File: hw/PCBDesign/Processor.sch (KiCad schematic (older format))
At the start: 39 parts, among them J4 Conn_ARM_JTAG_SWD_10, U11 74HC595, U13 STM32F446RETx, Y1 8MHz Crystal

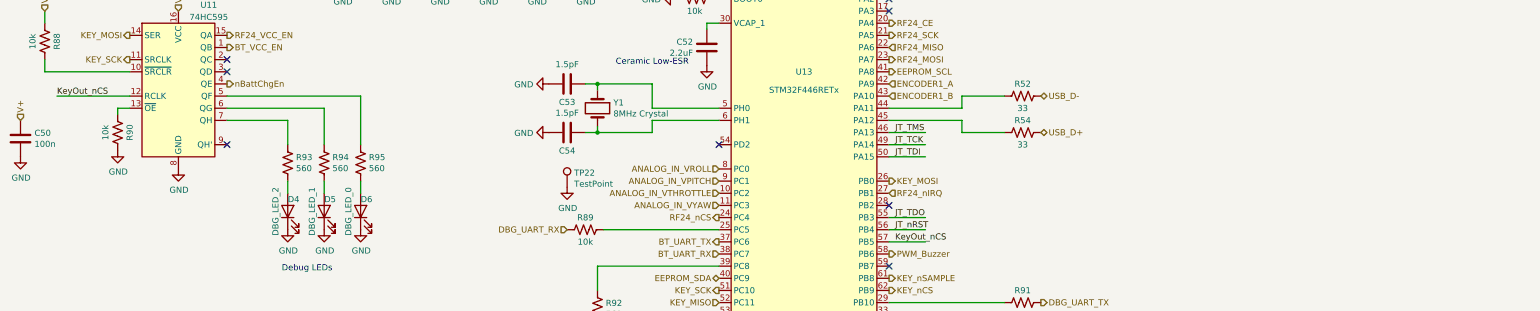
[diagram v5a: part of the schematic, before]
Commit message: Investigate some USB issues. Add PCB remarks for revision 2
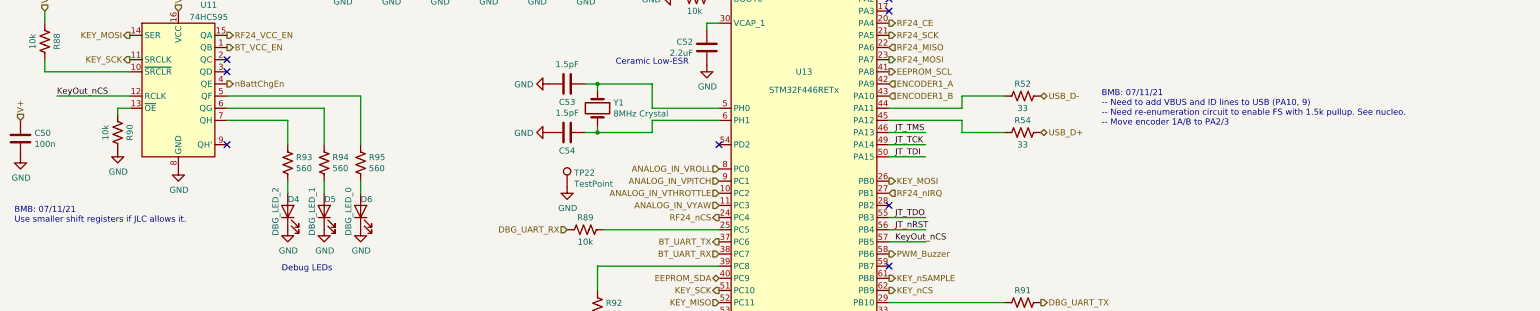
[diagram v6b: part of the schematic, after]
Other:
- note added: "BMB: 07/11/21\n-- Need to add VBUS and ID lines to USB (PA10, 9)\n-- Need re-enumeration circuit to enable FS with 1.5k pullup. See nucleo.\n-- Move encoder 1A/B to PA2/3"
- note added: "BMB: 07/11/21\nUse smaller shift registers if JLC allows it."
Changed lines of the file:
@@
 EELAYER 30 0
 EELAYER END
-$Descr A4 11693 8268
+$Descr A3 16535 11693
 encoding utf-8
 Sheet 11 11
@@
 Comment4 ""
 $EndDescr
-$Comp
-L MCU_ST_STM32F4:STM32F446RETx U13
-U 1 1 6047114C
-P 8100 2900
-F 0 "U13" H 8100 3600 50  0000 C CNN
-F 1 "STM32F446RETx" H 8100 3450 50  0000 C CNN
-F 2 "Package_QFP:LQFP-64_10x10mm_P0.5mm" H 7500 1200 50  0001 R CNN
-F 3 "http://www.st.com/st-web-ui/static/active/en/resource/technical/document/datasheet/DM00141306.pdf" H 8100 2900 50  0001 C CNN
-F 4 "C69336" H 8100 2900 50  0001 C CNN "LCSC"
-	1    8100 2900
-	1    0    0    -1
-$EndComp
 $Comp
 L Connector:Conn_ARM_JTAG_SWD_10 J4
@@
 Wire Wire Line
 	10200 6300 10200 6350
-$Comp
-L power:GND #PWR0106
-U 1 1 605ADCEE
-P 8100 4800
-F 0 "#PWR0106" H 8100 4550 50  0001 C CNN
-F 1 "GND" H 8105 4627 50  0000 C CNN
-F 2 "" H 8100 4800 50  0001 C CNN
-F 3 "" H 8100 4800 50  0001 C CNN
-	1    8100 4800
-	1    0    0    -1
-$EndComp
-Wire Wire Line
-	8100 4700 8100 4750
-Wire Wire Line
-	8100 4750 8200 4750
-Wire Wire Line
-	8200 4750 8200 4700
-Connection ~ 8100 4750
-Wire Wire Line
-	8100 4750 8100 4800
-Wire Wire Line
-	8200 4750 8300 4750
-Wire Wire Line
-	8300 4750 8300 4700
-Connection ~ 8200 4750
-Wire Wire Line
-	8100 4750 8000 4750
-Wire Wire Line
-	8000 4750 8000 4700
-Wire Wire Line
-	8000 4750 7900 4750
-Wire Wire Line
-	7900 4750 7900 4700
-Connection ~ 8000 4750
 Text Label 10750 5350 0    50   ~ 0
 JT_nRST
@@
 Text HLabel 8400 1100 1    50   Input ~ 0
 VDDA
-Wire Wire Line
-	8400 1100 8400 1200
 $Comp
 L Device:R_US R96
@@
 	9400 2500 8800 2500
 NoConn ~ 7400 4400
-NoConn ~ 7400 4500
 NoConn ~ 8800 3800
 NoConn ~ 8800 3300
@@
 NoConn ~ 3350 2200
 NoConn ~ 3350 2100
+Wire Wire Line
+	8400 1100 8400 1200
+NoConn ~ 7400 4500
+Connection ~ 8000 4750
+Wire Wire Line
+	7900 4750 7900 4700
+Wire Wire Line
+	8000 4750 7900 4750
+Wire Wire Line
+	8000 4750 8000 4700
+Wire Wire Line
+	8100 4750 8000 4750
+Connection ~ 8200 4750
+Wire Wire Line
+	8300 4750 8300 4700
+Wire Wire Line
+	8200 4750 8300 4750
+Wire Wire Line
+	8100 4750 8100 4800
+Connection ~ 8100 4750
+Wire Wire Line
+	8200 4750 8200 4700
+Wire Wire Line
+	8100 4750 8200 4750
+Wire Wire Line
+	8100 4700 8100 4750
+$Comp
+L power:GND #PWR0106
+U 1 1 605ADCEE
+P 8100 4800
+F 0 "#PWR0106" H 8100 4550 50  0001 C CNN
+F 1 "GND" H 8105 4627 50  0000 C CNN
+F 2 "" H 8100 4800 50  0001 C CNN
+F 3 "" H 8100 4800 50  0001 C CNN
+	1    8100 4800
+	1    0    0    -1
+$EndComp
+$Comp
+L MCU_ST_STM32F4:STM32F446RETx U13
+U 1 1 6047114C
+P 8100 2900
+F 0 "U13" H 8100 3600 50  0000 C CNN
+F 1 "STM32F446RETx" H 8100 3450 50  0000 C CNN
+F 2 "Package_QFP:LQFP-64_10x10mm_P0.5mm" H 7500 1200 50  0001 R CNN
+F 3 "http://www.st.com/st-web-ui/static/active/en/resource/technical/document/datasheet/DM00141306.pdf" H 8100 2900 50  0001 C CNN
+F 4 "C69336" H 8100 2900 50  0001 C CNN "LCSC"
+	1    8100 2900
+	1    0    0    -1
+$EndComp
+Text Notes 10550 2650 0    50   ~ 0
+BMB: 07/11/21\n-- Need to add VBUS and ID lines to USB (PA10, 9)\n-- Need re-enumeration circuit to enable FS with 1.5k pullup. See nucleo.\n-- Move encoder 1A/B to PA2/3
+Text Notes 1600 3450 0    50   ~ 0
+BMB: 07/11/21\nUse smaller shift registers if JLC allows it.
 $EndSCHEMATC

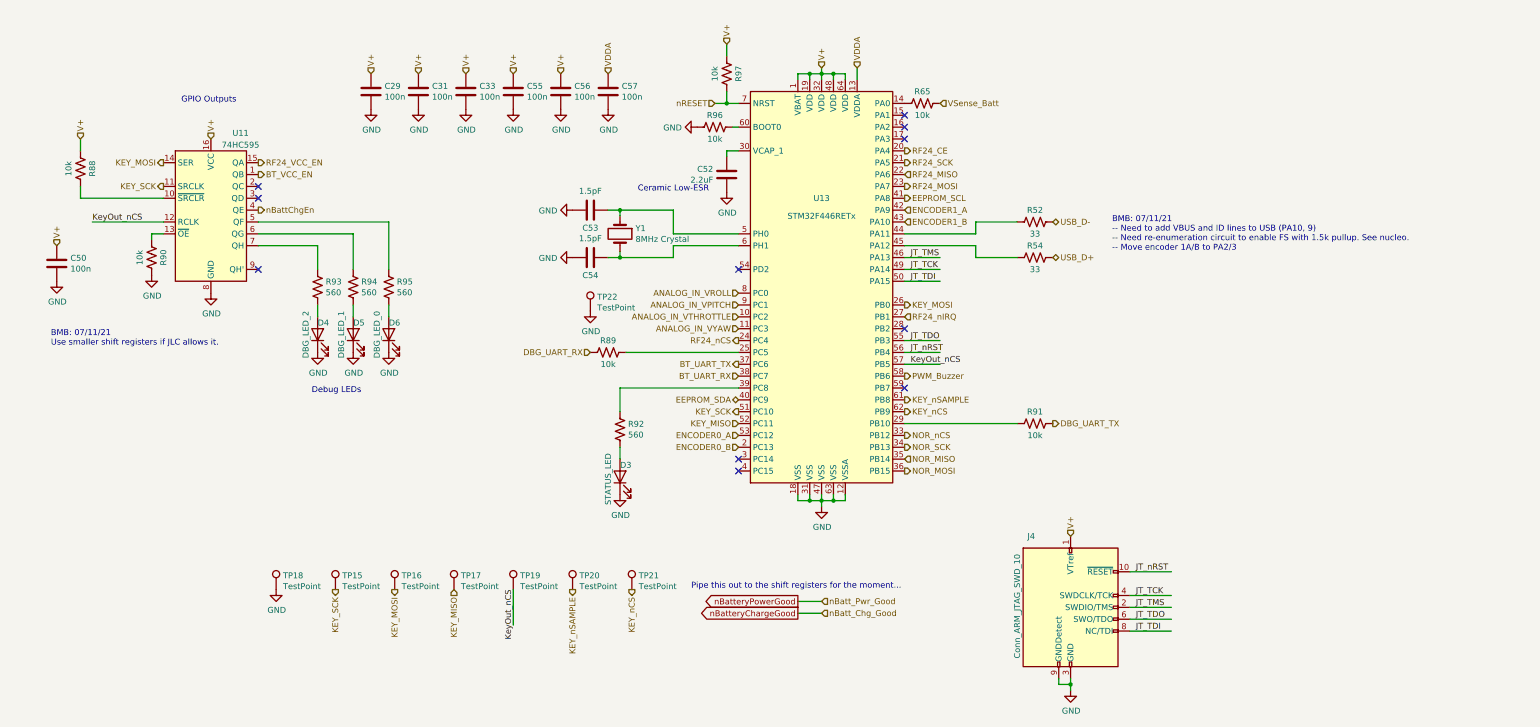
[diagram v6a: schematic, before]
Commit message: Start working on PCB rev 2.0
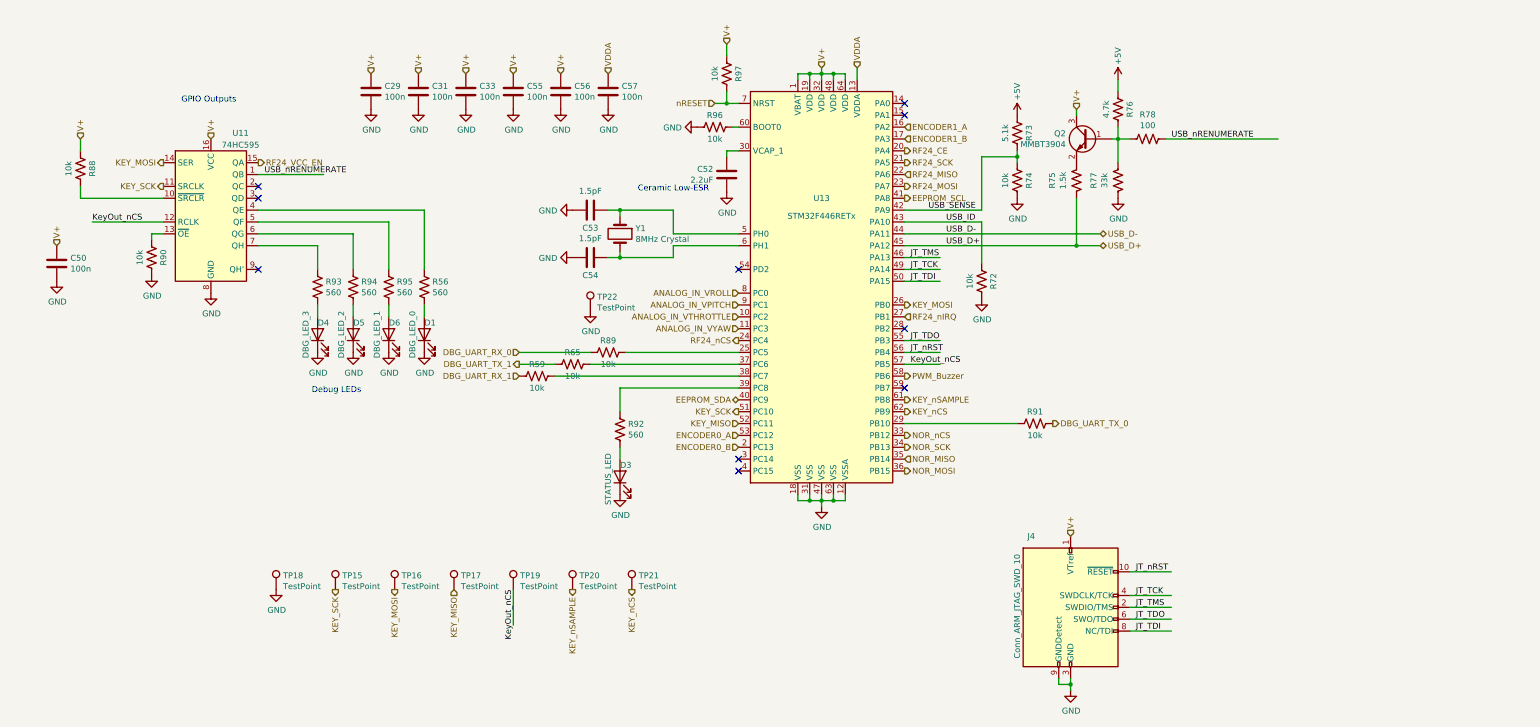
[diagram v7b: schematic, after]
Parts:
- removed R52, R54: 33, Resistor_SMD:R_0402_1005Metric, symbol Device:R_US
- added D1: DBG_LED_0, LED_SMD:LED_0603_1608Metric, symbol Device:LED
- added Q2: MMBT3904, Package_TO_SOT_SMD:SOT-23, symbol Transistor_BJT:MMBT3904
- added R56: 560, Resistor_SMD:R_0402_1005Metric, symbol Device:R_US
- added R59, R72, R74: 10k, Resistor_SMD:R_0402_1005Metric, symbol Device:R_US
- added R73: 5.1k, Resistor_SMD:R_0402_1005Metric, symbol Device:R_US
- added R75: 1.5k, Resistor_SMD:R_0402_1005Metric, symbol Device:R_US
- added R76: 4.7k, Resistor_SMD:R_0402_1005Metric, symbol Device:R_US
- added R77: 33k, Resistor_SMD:R_0402_1005Metric, symbol Device:R_US
- added R78: 100, Resistor_SMD:R_0402_1005Metric, symbol Device:R_US
- D4: value DBG_LED_2 -> DBG_LED_3
- D5: value DBG_LED_1 -> DBG_LED_2
- D6: value DBG_LED_0 -> DBG_LED_1
- J4: DigiKey (none) -> 609-3695-1-ND
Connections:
- net labels added: +5V, DBG_UART_RX_0, DBG_UART_RX_1, DBG_UART_TX_0, DBG_UART_TX_1, USB_ID, USB_SENSE, USB_nRENUMERATE
- net labels removed: BT_UART_RX, BT_UART_TX, BT_VCC_EN, DBG_UART_RX, DBG_UART_TX, VSense_Batt, nBattChgEn, nBatt_Chg_Good, nBatt_Pwr_Good, nBatteryChargeGood, nBatteryPowerGood
- wire segments 82 -> 100
- no-connect marks 11 -> 10
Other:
- note removed: "BMB: 07/11/21\n-- Need to add VBUS and ID lines to USB (PA10, 9)\n-- Need re-enumeration circuit to enable FS with 1.5k pullup. See nucleo.\n-- Move encoder 1A/B to PA2/3"
- note removed: "BMB: 07/11/21\nUse smaller shift registers if JLC allows it."
- note removed: "Pipe this out to the shift registers for the moment..."

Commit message: Add more work on PCB v2 design
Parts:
- removed TP15, TP16, TP17, TP18, TP19, TP20, TP21, TP22: TestPoint, TestPoint:TestPoint_Pad_2.5x2.5mm, symbol Connector:TestPoint
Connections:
- wire segments 100 -> 99
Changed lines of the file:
@@
 	6450 3500 7400 3500
-$Comp
-L Connector:TestPoint TP?
-U 1 1 605CFE2B
-P 3500 5500
-AR Path="/6045890B/605CFE2B" Ref="TP?"  Part="1"
-AR Path="/604707FB/605CFE2B" Ref="TP18"  Part="1"
-F 0 "TP18" H 3558 5618 50  0000 L CNN
-F 1 "TestPoint" H 3558 5527 50  0000 L CNN
-F 2 "TestPoint:TestPoint_Pad_2.5x2.5mm" H 3700 5500 50  0001 C CNN
-F 3 "~" H 3700 5500 50  0001 C CNN
-	1    3500 5500
-	1    0    0    -1
-$EndComp
-$Comp
-L power:GND #PWR09
-U 1 1 605D1BD5
-P 3500 5500
-F 0 "#PWR09" H 3500 5250 50  0001 C CNN
-F 1 "GND" H 3505 5327 50  0000 C CNN
-F 2 "" H 3500 5500 50  0001 C CNN
-F 3 "" H 3500 5500 50  0001 C CNN
-	1    3500 5500
-	1    0    0    -1
-$EndComp
-$Comp
-L Connector:TestPoint TP?
-U 1 1 605D1DEB
-P 4000 5500
-AR Path="/6045890B/605D1DEB" Ref="TP?"  Part="1"
-AR Path="/604707FB/605D1DEB" Ref="TP15"  Part="1"
-F 0 "TP15" H 4058 5618 50  0000 L CNN
-F 1 "TestPoint" H 4058 5527 50  0000 L CNN
-F 2 "TestPoint:TestPoint_Pad_2.5x2.5mm" H 4200 5500 50  0001 C CNN
-F 3 "~" H 4200 5500 50  0001 C CNN
-	1    4000 5500
-	1    0    0    -1
-$EndComp
-$Comp
-L Connector:TestPoint TP?
-U 1 1 605D20E0
-P 4500 5500
-AR Path="/6045890B/605D20E0" Ref="TP?"  Part="1"
-AR Path="/604707FB/605D20E0" Ref="TP16"  Part="1"
-F 0 "TP16" H 4558 5618 50  0000 L CNN
-F 1 "TestPoint" H 4558 5527 50  0000 L CNN
-F 2 "TestPoint:TestPoint_Pad_2.5x2.5mm" H 4700 5500 50  0001 C CNN
-F 3 "~" H 4700 5500 50  0001 C CNN
-	1    4500 5500
-	1    0    0    -1
-$EndComp
-$Comp
-L Connector:TestPoint TP?
-U 1 1 605D227A
-P 5000 5500
-AR Path="/6045890B/605D227A" Ref="TP?"  Part="1"
-AR Path="/604707FB/605D227A" Ref="TP17"  Part="1"
-F 0 "TP17" H 5058 5618 50  0000 L CNN
-F 1 "TestPoint" H 5058 5527 50  0000 L CNN
-F 2 "TestPoint:TestPoint_Pad_2.5x2.5mm" H 5200 5500 50  0001 C CNN
-F 3 "~" H 5200 5500 50  0001 C CNN
-	1    5000 5500
-	1    0    0    -1
-$EndComp
-$Comp
-L Connector:TestPoint TP?
-U 1 1 605D23A2
-P 5500 5500
-AR Path="/6045890B/605D23A2" Ref="TP?"  Part="1"
-AR Path="/604707FB/605D23A2" Ref="TP19"  Part="1"
-F 0 "TP19" H 5558 5618 50  0000 L CNN
-F 1 "TestPoint" H 5558 5527 50  0000 L CNN
-F 2 "TestPoint:TestPoint_Pad_2.5x2.5mm" H 5700 5500 50  0001 C CNN
-F 3 "~" H 5700 5500 50  0001 C CNN
-	1    5500 5500
-	1    0    0    -1
-$EndComp
-Text HLabel 4500 5500 3    50   Output ~ 0
-KEY_MOSI
-Text HLabel 5000 5500 3    50   Input ~ 0
-KEY_MISO
-Text HLabel 4000 5500 3    50   Output ~ 0
-KEY_SCK
-Text Label 5500 5500 3    50   ~ 0
-KeyOut_nCS
-Wire Wire Line
-	5500 5500 5500 5800
-$Comp
-L Connector:TestPoint TP?
-U 1 1 605D756E
-P 6000 5500
-AR Path="/6045890B/605D756E" Ref="TP?"  Part="1"
-AR Path="/604707FB/605D756E" Ref="TP20"  Part="1"
-F 0 "TP20" H 6058 5618 50  0000 L CNN
-F 1 "TestPoint" H 6058 5527 50  0000 L CNN
-F 2 "TestPoint:TestPoint_Pad_2.5x2.5mm" H 6200 5500 50  0001 C CNN
-F 3 "~" H 6200 5500 50  0001 C CNN
-	1    6000 5500
-	1    0    0    -1
-$EndComp
-Text HLabel 6000 5500 3    50   Output ~ 0
-KEY_nSAMPLE
-$Comp
-L Connector:TestPoint TP?
-U 1 1 605D9B3F
-P 6500 5500
-AR Path="/6045890B/605D9B3F" Ref="TP?"  Part="1"
-AR Path="/604707FB/605D9B3F" Ref="TP21"  Part="1"
-F 0 "TP21" H 6558 5618 50  0000 L CNN
-F 1 "TestPoint" H 6558 5527 50  0000 L CNN
-F 2 "TestPoint:TestPoint_Pad_2.5x2.5mm" H 6700 5500 50  0001 C CNN
-F 3 "~" H 6700 5500 50  0001 C CNN
-	1    6500 5500
-	1    0    0    -1
-$EndComp
-Text HLabel 6500 5500 3    50   Output ~ 0
-KEY_nCS
-$Comp
-L Connector:TestPoint TP?
-U 1 1 605E052A
-P 6150 3150
-AR Path="/6045890B/605E052A" Ref="TP?"  Part="1"
-AR Path="/604707FB/605E052A" Ref="TP22"  Part="1"
-F 0 "TP22" H 6208 3268 50  0000 L CNN
-F 1 "TestPoint" H 6208 3177 50  0000 L CNN
-F 2 "TestPoint:TestPoint_Pad_2.5x2.5mm" H 6350 3150 50  0001 C CNN
-F 3 "~" H 6350 3150 50  0001 C CNN
-	1    6150 3150
-	1    0    0    -1
-$EndComp
-$Comp
-L power:GND #PWR012
-U 1 1 605E0530
-P 6150 3150
-F 0 "#PWR012" H 6150 2900 50  0001 C CNN
-F 1 "GND" H 6155 2977 50  0000 C CNN
-F 2 "" H 6150 3150 50  0001 C CNN
-F 3 "" H 6150 3150 50  0001 C CNN
-	1    6150 3150
-	1    0    0    -1
-$EndComp
 $Comp
 L Device:LED D3
